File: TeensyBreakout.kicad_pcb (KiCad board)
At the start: 2 copper layers, 116.5 x 115.1 mm, 112 parts, among them CON2 Headphone, CON3 Line In, IC1 ZLDO1117G33, IC2 NCP1117ST50T3G, J1 73725-0110BLF, J2 Conn_01x04, J3 RJ45_LED, J4 PJ-102A, J5 OSTTC022162 (R), J6 OSTTC022162 (L), Q1 FDN340P, Q1A1 BSD223P, Q1B1 BSD223P, Q6 BC107, SW1 SW_MEC_5E, U1 Teensy4.1, U5 SGTL5000XNAA3, U6 TDA7265

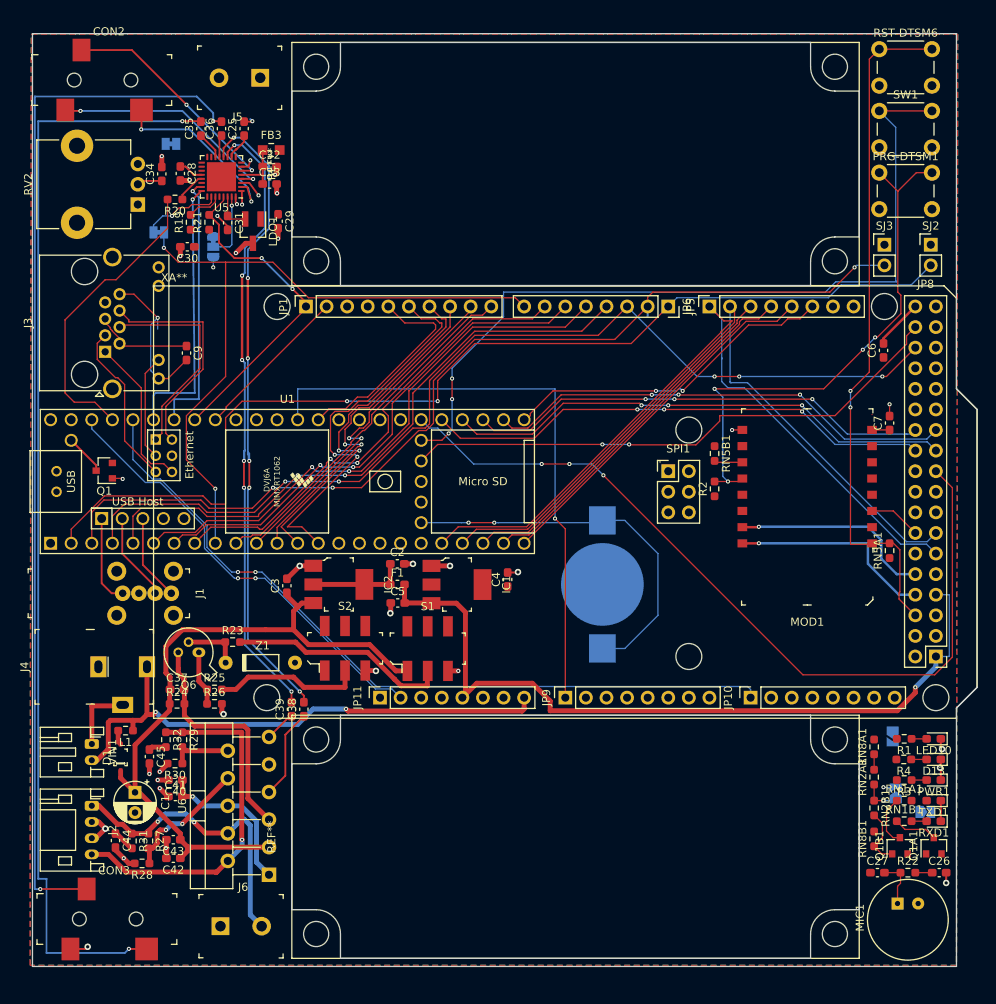
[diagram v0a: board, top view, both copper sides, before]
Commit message: made more room for speakers and corrected rotation of furthest headers
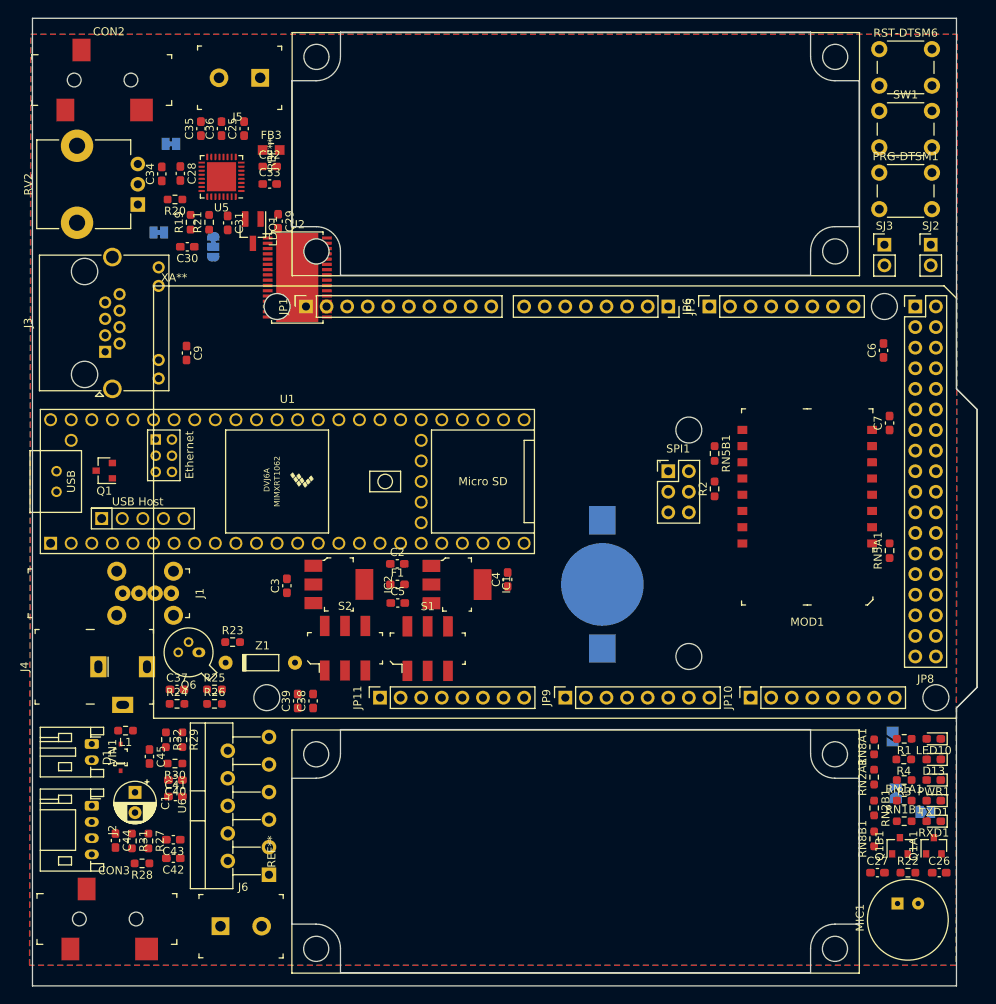
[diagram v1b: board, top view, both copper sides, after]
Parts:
- removed the REF** at (42.0, 51.0)
- removed the REF** at (42.0, 134.0)
- added REF**: AIYIMA 3070 Speaker, CustomFootprints:AIYIMA 3070 Speaker, F.Cu at (42.0, 49.8)
- added REF**: AIYIMA 3070 Speaker, CustomFootprints:AIYIMA 3070 Speaker, F.Cu at (42.0, 135.8)
- added U2: TPA3126D2, Package_SO:HTSSOP-32-1EP_6.1x11mm_P0.65mm_EP5.2x11mm_Mask4.11x4.36mm, F.Cu at (45.7, 65.0)
- moved JP8 43.3 mm to (121.9, 111.8), turned to 180 degrees
- moved C38 1.53 mm to (47.6, 117.2)
- moved C39 1.27 mm to (45.7, 117.2)
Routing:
- net Net-(C35-Pad2): track 136.3 -> 0.00 mm, vias 2 -> 0
- net /D0-RX1-CS1-CRX2: track 129.8 -> 0.00 mm, vias 2 -> 0
- net Net-(C36-Pad2): track 129.1 -> 0.00 mm, vias 2 -> 0
- net /D2-OUT2: track 122.1 -> 0.00 mm, vias 5 -> 0
- net /D1-TX1-MISO1-CTX2: track 120.1 -> 0.00 mm, vias 3 -> 0
- net /D38-A14-CS1-IN1: track 103.3 -> 0.00 mm, vias 3 -> 0
- net /ON-OFF: track 101.5 -> 0.00 mm, vias 3 -> 0
- net /5V_FUSE: track 97.1 -> 0.00 mm, vias 1 -> 0
- net /D28-RX7: track 96.0 -> 0.00 mm
- net /D22-A8-CTX1: track 95.4 -> 0.00 mm, vias 2 -> 0
- net /D29-TX7: track 90.5 -> 0.00 mm
- net /D7-RX2-OUT1A: track 87.5 -> 0.00 mm, vias 2 -> 0
- net /VIN: track 85.1 -> 0.00 mm
- net /ESP-RST: track 84.5 -> 0.00 mm, vias 2 -> 0
- net /AmpV2/LINEIN_L: track 80.3 -> 0.00 mm, vias 6 -> 0
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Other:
- board size 116.5 x 115.1 mm -> 116.5 x 119.4 mm

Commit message: lots of wires left
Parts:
- removed U2: TPA3126D2, Package_SO:HTSSOP-32-1EP_6.1x11mm_P0.65mm_EP5.2x11mm_Mask4.11x4.36mm
- moved C38 71.7 mm to (35.3, 46.6), turned to 270 degrees
- moved C39 71.1 mm to (37.1, 46.6), turned to 270 degrees
- moved C7 29.3 mm to (97.4, 103.0), turned to 270 degrees
- moved BT1 25.5 mm to (107.4, 94.7), turned to 180 degrees
- moved RN5B1 25.2 mm to (119.0, 99.2), turned to 90 degrees
- moved RN5A1 23.3 mm to (97.4, 89.3), turned to 270 degrees
- moved R2 22.2 mm to (119.0, 94.8), turned to 270 degrees
- moved JP13 17.5 mm to (38.4, 63.9), turned to 90 degrees
- moved JP12 13.7 mm to (41.6, 63.9), turned to 90 degrees
- moved MOD1 4.44 mm to (107.6, 95.1), turned to 0 degrees
- moved C36 2.79 mm to (33.5, 46.6)
- moved C35 2.03 mm to (31.8, 46.6)
- moved Q1 1.69 mm to (20.2, 88.6)
- moved C6 1.13 mm to (119.1, 74.1), turned to 270 degrees
- moved C44 0.05 mm to (23.2, 134.5), turned to 90 degrees
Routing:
- net /D23-A9-CRX1-MCLK1: track 0.00 -> 150.2 mm, vias 0 -> 7
- net /D19-A5-SCL0: track 0.00 -> 146.6 mm, vias 0 -> 7
- net /D0-RX1-CS1-CRX2: track 0.00 -> 140.0 mm, vias 0 -> 5
- net /D1-TX1-MISO1-CTX2: track 0.00 -> 132.2 mm, vias 0 -> 4
- net /D15-A1-RX3-SPDIF_IN: track 0.00 -> 119.4 mm, vias 0 -> 7
- net /D18-A4-SDA0: track 0.00 -> 119.0 mm, vias 0 -> 5
- net /D22-A8-CTX1: track 0.00 -> 108.2 mm, vias 0 -> 3
- net /D21-A7-RX5-BCLK1: track 0.00 -> 102.8 mm, vias 0 -> 5
- net /D20-A6-TX5-LRCLK1: track 0.00 -> 99.7 mm, vias 0 -> 5
- net /D2-OUT2: track 0.00 -> 94.0 mm, vias 0 -> 3
- net /D12-MISO-MQSL: track 0.00 -> 90.9 mm, vias 0 -> 6
- net /D3-LRCLK2: track 0.00 -> 89.2 mm, vias 0 -> 3
- net /D4-BCLK2: track 0.00 -> 83.8 mm, vias 0 -> 3
- net /VIN: track 0.00 -> 83.4 mm
- net /PGM: track 0.00 -> 82.6 mm, vias 0 -> 2
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
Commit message: progress
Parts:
- moved BT1 1.94 mm to (105.8, 93.7)
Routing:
- net /5V_FUSE: track 20.5 -> 220.4 mm, vias 0 -> 5
- net /ON-OFF: track 8.02 -> 152.7 mm, vias 0 -> 4
- net /D11-MOSI-CTX1: track 45.2 -> 136.8 mm, vias 5 -> 8
- net /D10-CS-MQSR: track 49.4 -> 137.8 mm, vias 4 -> 6
- net /D39-A15-MISO1-OUT1A: track 0.00 -> 83.8 mm, vias 0 -> 1
- net /D40-A16: track 0.00 -> 83.0 mm, vias 0 -> 1
- net /D9-OUT1C: track 54.4 -> 137.2 mm, vias 4 -> 6
- net /D37-CS-PWM: track 0.00 -> 78.5 mm, vias 0 -> 1
- net /D38-A14-CS1-IN1: track 0.00 -> 78.2 mm, vias 0 -> 1
- net /D13-SCK-LED: track 67.9 -> 142.5 mm, vias 1 -> 4
- net /D2-OUT2: track 94.0 -> 168.5 mm, vias 3 -> 5
- net /D35-TX8: track 0.00 -> 72.9 mm
- net /D36-CS-PWM: track 0.00 -> 72.5 mm, vias 0 -> 1
- net /D6-OUT1D: track 0.00 -> 72.5 mm, vias 0 -> 4
- net /D7-RX2-OUT1A: track 0.00 -> 71.0 mm, vias 0 -> 2
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
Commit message: finished traces
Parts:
- moved Q1 1.33 mm to (21.5, 88.6)
- moved FB3 0.36 mm to (42.5, 48.9)
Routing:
- net Net-(C27-Pad1): track 0.00 -> 228.9 mm, vias 0 -> 2
- net Net-(C26-Pad1): track 2.08 -> 226.1 mm, vias 0 -> 2
- net Net-(C39-Pad1): track 0.00 -> 141.5 mm, vias 0 -> 9
- net Net-(C38-Pad1): track 0.00 -> 135.8 mm, vias 0 -> 7
- net Net-(C35-Pad2): track 0.00 -> 129.9 mm, vias 0 -> 6
- net Net-(J2-Pad4): track 46.1 -> 163.7 mm, vias 1 -> 4
- net Net-(C36-Pad2): track 0.00 -> 117.5 mm, vias 0 -> 6
- net /D8-TX2-IN1: track 35.6 -> 67.3 mm, vias 3 -> 6
- net /VBAT: track 39.4 -> 62.7 mm, vias 0 -> 2
- net GND: track 68.8 -> 87.5 mm, vias 35 -> 36
- net Net-(CON2-Pad2): track 24.8 -> 29.9 mm
- net /D21-A7-RX5-BCLK1: track 130.3 -> 134.0 mm, vias 6 -> 10
- net +3V3: track 15.8 -> 13.5 mm
- net /TEENSY_3V3: track 76.0 -> 73.9 mm
- net Net-(JP13-Pad2): track 10.1 -> 12.1 mm
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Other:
- board size 116.5 x 119.4 mm -> 116.8 x 119.4 mm
